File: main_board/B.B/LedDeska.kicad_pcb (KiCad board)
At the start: 4 copper layers, 92 x 92 mm, 136 parts, among them J3 Conn_01x11, U1 WS2812, U10 WS2812, U11 WS2812, U12 WS2812, U13 WS2812, U14 WS2812, U15 WS2812, U16 WS2812, U17 WS2812, U18 WS2812, U19 WS2812, U2 WS2812, U20 WS2812, U21 WS2812, U22 WS2812, U23 WS2812, U24 WS2812, U25 WS2812, U26 WS2812, U27 WS2812, U28 WS2812, U29 WS2812, U3 WS2812, U30 WS2812, U31 WS2812, U32 WS2812, U33 WS2812, U34 WS2812, U35 WS2812, U36 WS2812, U37 WS2812, U38 WS2812, U39 WS2812, U4 WS2812, U40 WS2812, U41 WS2812, U42 WS2812, U43 WS2812, U44 WS2812, U45 WS2812, U46 WS2812, U47 WS2812, U48 WS2812, U49 WS2812, U5 WS2812, U50 WS2812, U51 WS2812, U52 WS2812, U53 WS2812, U54 WS2812, U55 WS2812, U56 WS2812, U57 WS2812, U58 WS2812, U59 WS2812, U6 WS2812, U60 WS2812, U66 LDC1314, U7 WS2812, U8 WS2812, U9 WS2812

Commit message: presuny_konektoru
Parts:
- added J7: Conn_01x03, Connector_PinHeader_2.54mm:PinHeader_1x03_P2.54mm_Vertical, B.Cu at (91.6, 73.6)
- moved C83 4.35 mm to (94.2, 76.4)
- moved C82 1.68 mm to (94.1, 67.1)
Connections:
- U60 pad 2: Net-(U60-Pad2) -> /next-board00/WS281200/DOUT
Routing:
- net /next-board00/WS281200/DOUT: track 0.00 -> 13.3 mm, vias 0 -> 1
- net /next-board00/5V: track 297.9 -> 307.1 mm
- net /next-board00/GND: track 10.1 -> 11.6 mm
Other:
- copper layers 4 -> 2

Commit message: new schema
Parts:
- moved J7 2.70 mm to (88.9, 73.6)
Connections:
- J7 pad 1: /next-board00/5V -> /next-board00/WS281200/DOUT
- J7 pad 2: /next-board00/WS281200/DOUT -> /next-board00/5V
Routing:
- net /next-board00/GND: track 11.6 -> 14.3 mm
- net /next-board00/WS281200/DOUT: track 13.3 -> 15.6 mm
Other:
- board size 92 x 92 mm -> 94 x 95 mm

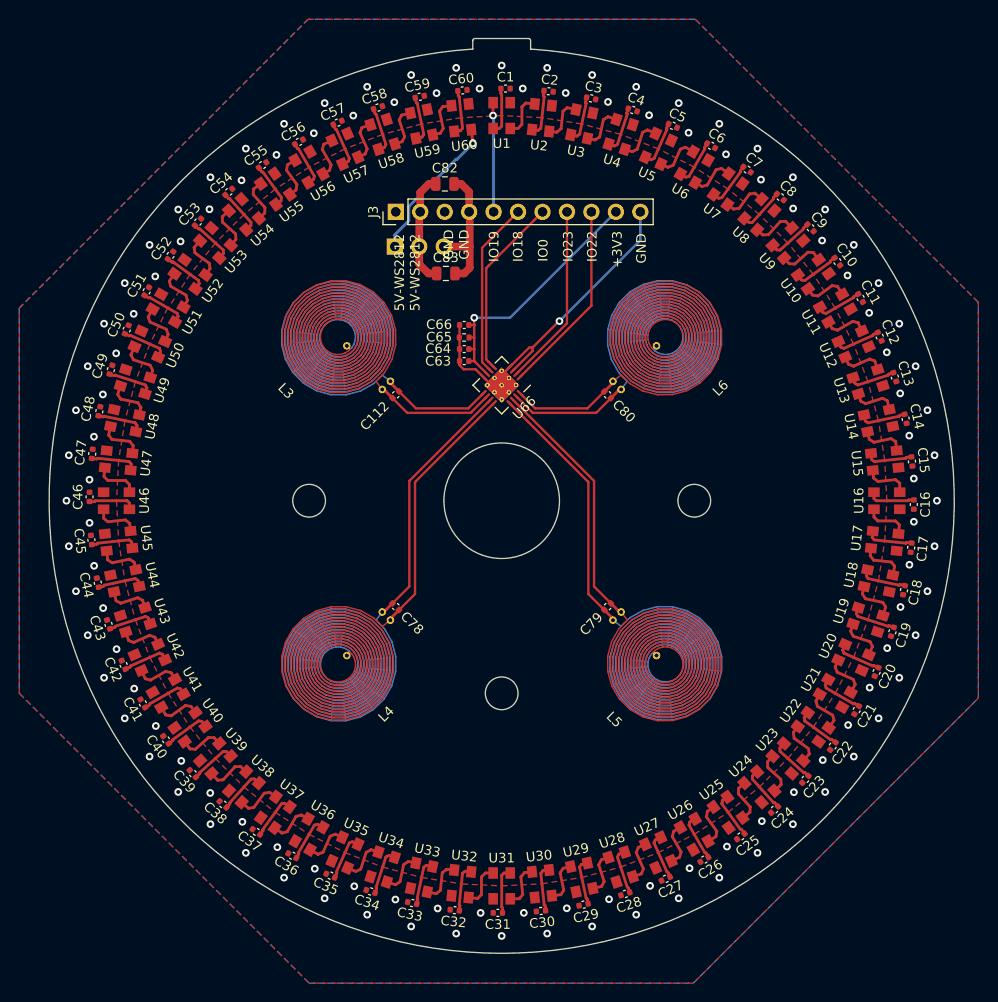
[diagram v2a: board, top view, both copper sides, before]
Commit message: vymena rezistoru pro snimani nabijeciho proudu
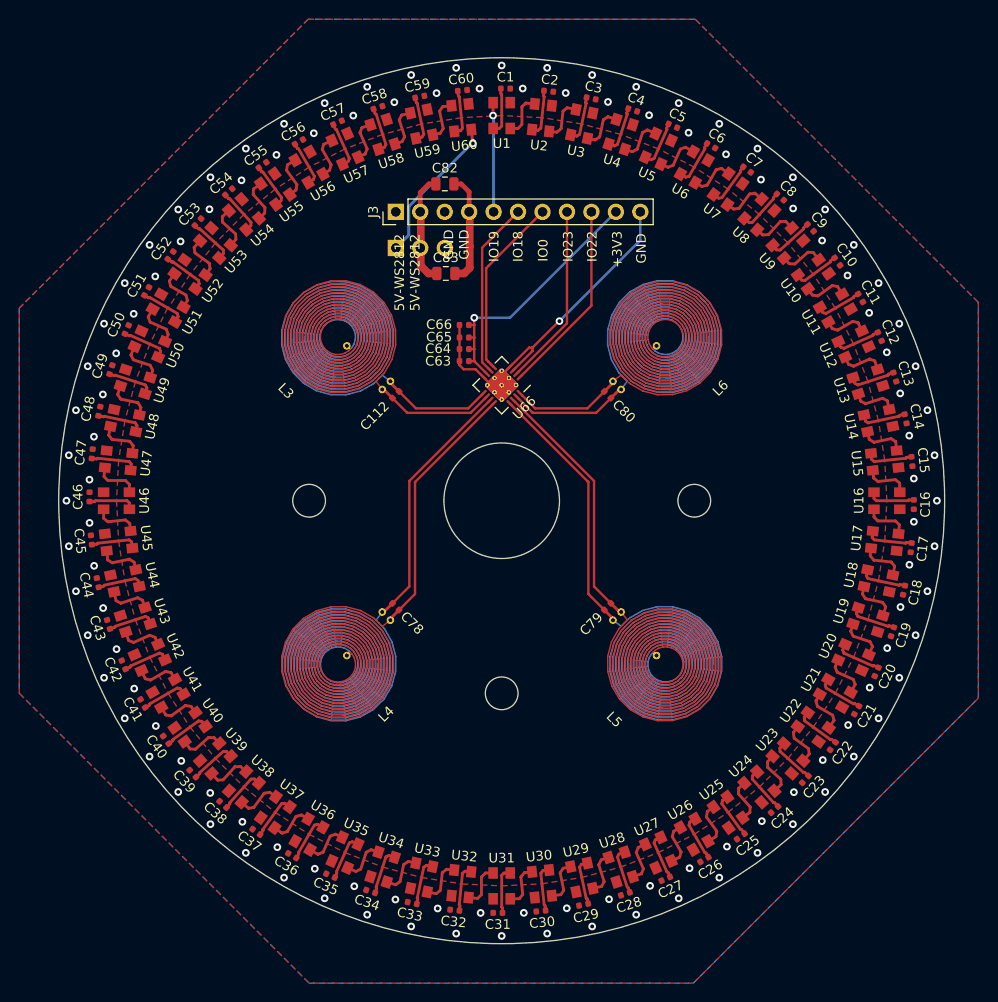
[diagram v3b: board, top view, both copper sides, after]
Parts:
- moved J7 0.19 mm to (89.0, 73.8)
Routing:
- net /next-board00/GND: track 14.3 -> 11.6 mm
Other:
- board size 94 x 95 mm -> 92 x 92 mm
- copper layers 2 -> 4
